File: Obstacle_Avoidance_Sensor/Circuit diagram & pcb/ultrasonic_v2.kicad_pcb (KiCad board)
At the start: 2 copper layers, 59.8 x 53.5 mm, 7 parts, among them J1 Conn_01x03, J2 Conn_01x02, J3 Conn_01x04

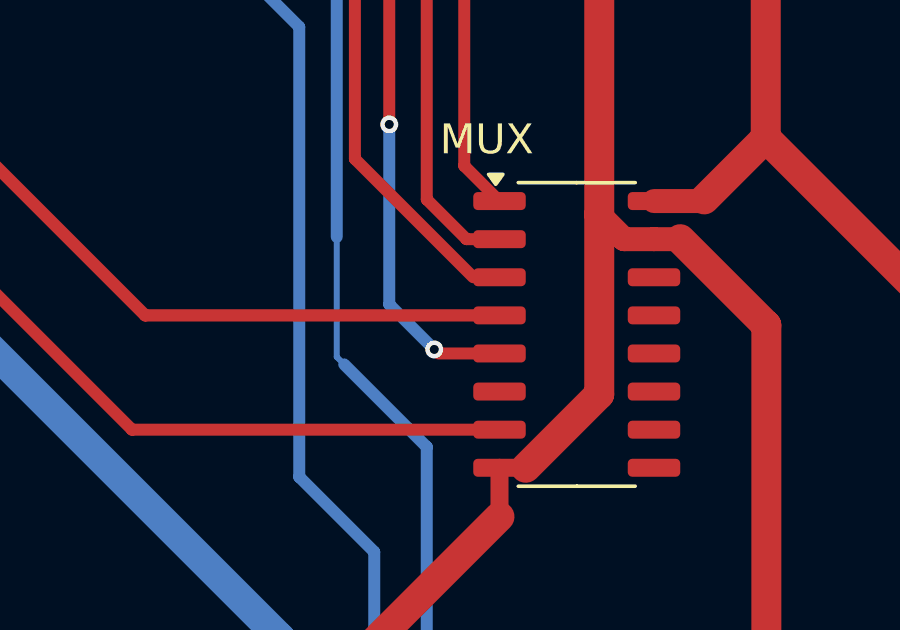
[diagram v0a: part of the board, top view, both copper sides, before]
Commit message: CarrierAssistant 추가
물건들기보조기기
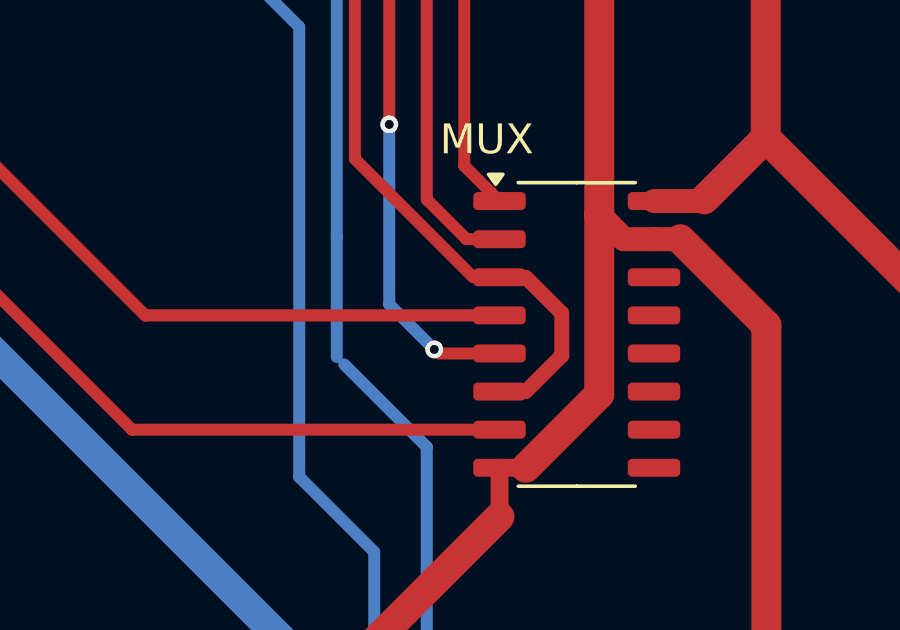
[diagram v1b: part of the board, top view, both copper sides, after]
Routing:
- net Net-(A1-D7): track 25.2 -> 31.8 mm
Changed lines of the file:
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@@
 			(drillshape 0)
 			(scaleselection 1)
-			(outputdirectory "gerber/")
+			(outputdirectory "../241118/")
 		)
 	)
@@
 		(start 156.5 74.25)
 		(end 156.5 70.25)
-		(width 0.2)
+		(width 0.4)
 		(layer "B.Cu")
 		(net 34)
@@
 	)
 	(segment
+		(start 164 72.795001)
+		(end 164 74.204999)
+		(width 0.5)
+		(layer "F.Cu")
+		(net 42)
+	)
+	(segment
+		(start 162.799999 71.595)
+		(end 164 72.795001)
+		(width 0.5)
+		(layer "F.Cu")
+		(net 42)
+	)
+	(segment
+		(start 164 74.204999)
+		(end 162.799999 75.405)
+		(width 0.5)
+		(layer "F.Cu")
+		(net 42)
+	)
+	(segment
+		(start 162.799999 75.405)
+		(end 161.925 75.405)
+		(width 0.2)
+		(layer "F.Cu")
+		(net 42)
+	)
+	(segment
 		(start 161.050001 71.595)
 		(end 161.925 71.595)
 		(width 0.2)
 		(layer "F.Cu")
+		(net 42)
+	)
+	(segment
+		(start 161.925 71.595)
+		(end 162.799999 71.595)
+		(width 0.2)
+		(layer "F.Cu")
